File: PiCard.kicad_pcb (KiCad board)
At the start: 4 copper layers, 81 x 50 mm, 53 parts, among them J1 Usb Data Jumper, J2 USB_C_Receptacle_USB2.0_16P, J6 Micro_SD_Card_Det2, J7 nRPIBOOT Jumper, M2_3V3 TestPoint, U1 TPD4EUSB30, U3 TPD4EUSB30, U4 TPD4EUSB30, U5 MAX3232, U6 RT9742GGJ5, U7 TPS82130

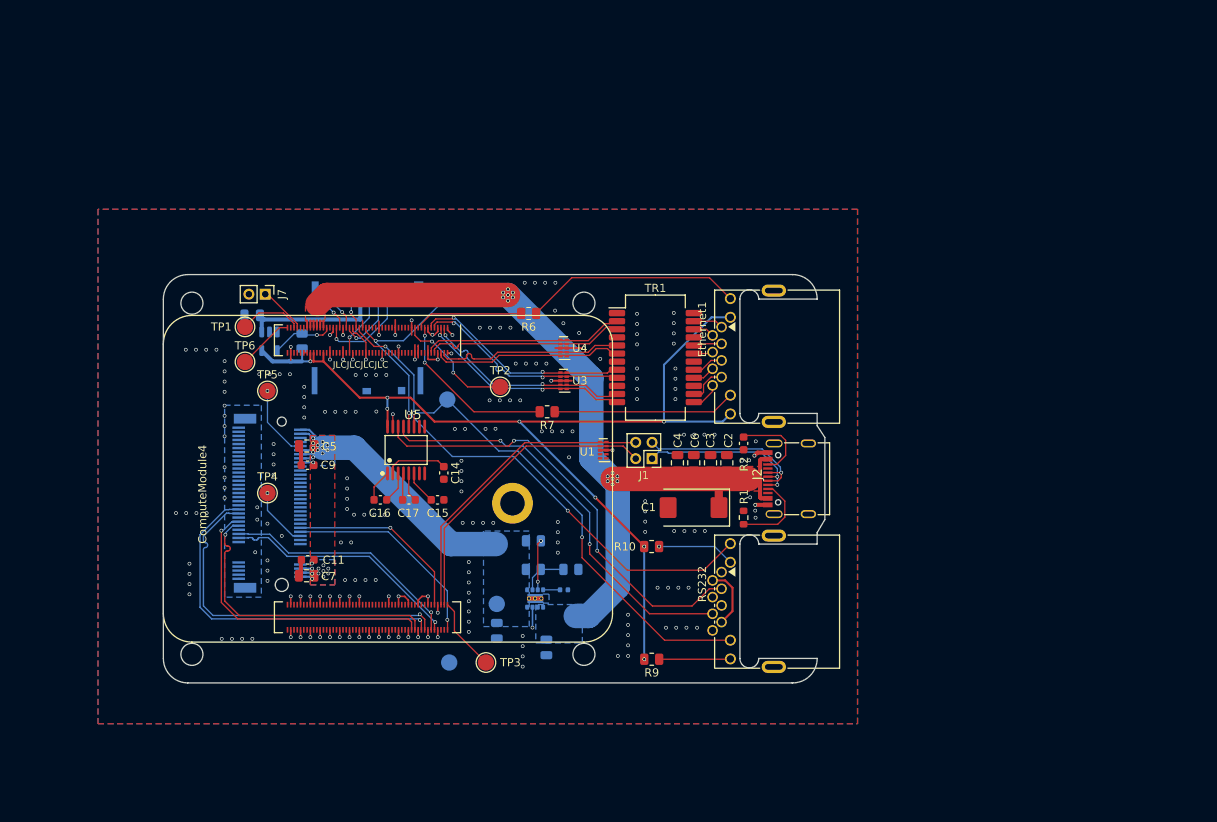
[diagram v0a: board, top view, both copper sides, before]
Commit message: Fix ethernet wiring order
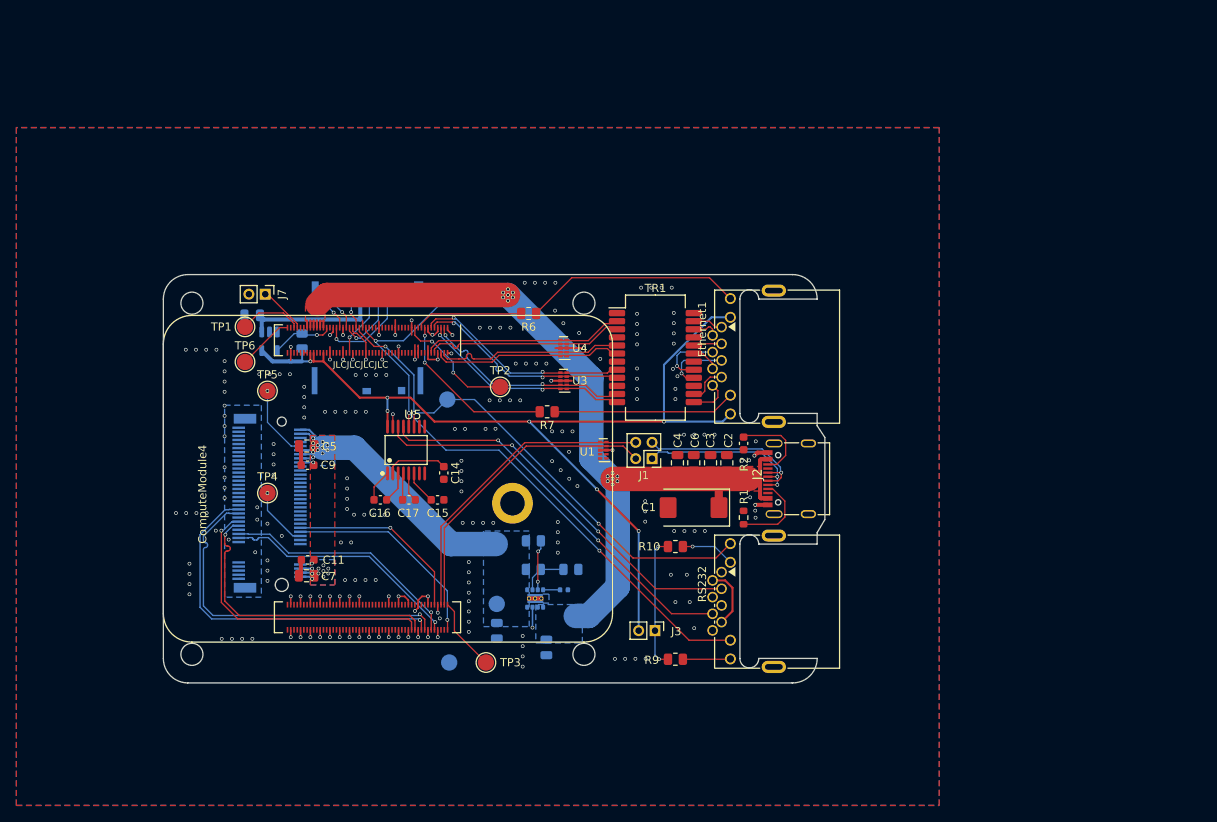
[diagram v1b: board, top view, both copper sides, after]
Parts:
- added J3: UART Activity Jumper, Connector_PinHeader_2.00mm:PinHeader_1x02_P2.00mm_Vertical, F.Cu at (120.2, 118.6)
- moved R10 2.91 mm to (122.7, 108.3), turned to 180 degrees
- moved R9 2.90 mm to (122.7, 122.1), turned to 0 degrees
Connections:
- net Net-(TR1-MX1+) renamed /Module A/DA_P
- net Net-(TR1-MX1-) renamed /Module A/DA_N
- net Net-(TR1-MX2+) renamed /Module A/DB_P
- net Net-(TR1-MX4+) renamed /Module A/DD_P
- net Net-(TR1-MX4-) renamed /Module A/DD_N
- Ethernet1 pad 4: Net-(TR1-MX2-) -> /Module A/DC_P
- Ethernet1 pad 5: Net-(TR1-MX3+) -> /Module A/DC_N
- Ethernet1 pad 6: Net-(TR1-MX3-) -> /Module A/DB_N
- R10 pad 1: +3.3V -> Net-(R10-Pad1)
- R10 pad 2: Net-(R10-Pad2) -> Net-(J3-Pin_1)
- R9 pad 1: Net-(R9-Pad1) -> Net-(J3-Pin_1)
- R9 pad 2: +3.3V -> Net-(R9-Pad2)
- RS232 pad 10: Net-(R9-Pad1) -> Net-(R9-Pad2)
- RS232 pad 11: /Module A/GPIO15_UART_RX -> /Module A/GPIO14_UART_TX
- RS232 pad 12: Net-(R10-Pad2) -> Net-(R10-Pad1)
- RS232 pad 9: /Module A/GPIO14_UART_TX -> /Module A/GPIO15_UART_RX
- TR1 pad 16: Net-(TR1-MX3-) -> /Module A/DC_N
- TR1 pad 17: Net-(TR1-MX3+) -> /Module A/DC_P
- TR1 pad 19: Net-(TR1-MX2-) -> /Module A/DB_N
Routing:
- net Net-(J3-Pin_1): track 0.00 -> 16.4 mm, vias 0 -> 2
- net Net-(R10-Pad2): track 9.53 -> 0.00 mm, vias 1 -> 0
- net Net-(R9-Pad1): track 8.78 -> 0.00 mm
- net /Module A/DC_P: track 0.00 -> 8.05 mm, vias 0 -> 1
- net /Module A/DC_N: track 0.00 -> 8.04 mm, vias 0 -> 1
- net Net-(R10-Pad1): track 0.00 -> 6.62 mm, vias 0 -> 1
- net /Module A/GPIO14_UART_TX: track 70.4 -> 63.9 mm
- net Net-(R9-Pad2): track 0.00 -> 5.88 mm
- net /Module A/RS232_TXD: track 53.9 -> 48.5 mm
- net +3.3V: track 122.7 -> 118.4 mm, vias 8 -> 7
- net Net-(TR1-MX3+): track 3.87 -> 0.00 mm
- net /Module A/DB_N: track 0.00 -> 3.45 mm
- net /Module A/RS232_RXD: track 50.9 -> 47.9 mm
- net Net-(TR1-MX3-): track 2.76 -> 0.00 mm
- net Net-(TR1-MX2-): track 2.37 -> 0.00 mm
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
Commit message: Clean up schematics
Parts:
- removed Ethernet1: Ethernet, PiCard:RJ45-TH_MJ88B-B011-RVL11-P
- removed PCIe1: Bus_M.2_Socket_M, PiCard:CONN-SMD_APCI0146-P001A
- removed RS232: RS232, PiCard:RJ45-TH_MJ88B-B011-RVL11-P
- added J4: Bus_M.2_Socket_M, PiCard:CONN-SMD_APCI0146-P001A, B.Cu at (73.0, 103.0)
- added J5: Ethernet, PiCard:RJ45-TH_MJ88B-B011-RVL11-P, F.Cu at (131.0, 85.0)
- added J8: RS232, PiCard:RJ45-TH_MJ88B-B011-RVL11-P, F.Cu at (131.0, 115.0)
- C11, C14, C15, C16, C17, C9: value 0.1uF -> 100nF
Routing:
- net Net-(RS232-Pad2): track 7.57 -> 0.00 mm
- net Net-(J8-Pad2): track 0.00 -> 7.57 mm

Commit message: PiCard v2
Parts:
- removed +5V1, GND1, GPIO14, GPIO15, M2_3V3, TP1, TP2, TP3, TP4, TP5, TP6: TestPoint, TestPoint:TestPoint_Pad_D2.0mm
- removed ComputeModule4: ComputeModule4-CM4, PiCard:Raspberry-Pi-4-Compute-Module
- removed J7: nRPIBOOT Jumper, Connector_PinHeader_2.00mm:PinHeader_1x02_P2.00mm_Vertical
- added BT1: RTC Battery, PiCard:BAT-SMD_MY-1220-03, F.Cu at (106.0, 90.0)
- added C13: 100n, Capacitor_SMD:C_0402_1005Metric, B.Cu at (163.2, 82.9)
- added C19: 22u, Capacitor_SMD:C_0805_2012Metric, B.Cu at (149.0, 71.5)
- added C20: 22u, Capacitor_SMD:C_0805_2012Metric, B.Cu at (151.7, 74.5)
- added C21: 430pF, Capacitor_SMD:C_0402_1005Metric, B.Cu at (146.5, 72.0)
- added C22: 100n, Capacitor_SMD:C_0402_1005Metric, B.Cu at (106.5, 92.5)
- added C23: 47u, Capacitor_SMD:C_0805_2012Metric, B.Cu at (113.0, 82.3)
- added C24: 47u, Capacitor_SMD:C_0805_2012Metric, B.Cu at (117.2, 72.9)
- added C25: 100n, Capacitor_SMD:C_0402_1005Metric, B.Cu at (119.4, 72.9)
- added C26: 100n, Capacitor_SMD:C_0402_1005Metric, B.Cu at (124.5, 72.9)
- added C27: 100n, Capacitor_SMD:C_0402_1005Metric, B.Cu at (113.5, 77.7)
- added C28: 100n, Capacitor_SMD:C_0402_1005Metric, B.Cu at (113.5, 76.7)
- added C29: 100n, Capacitor_SMD:C_0402_1005Metric, B.Cu at (133.0, 75.0)
- added C30: 100n, Capacitor_SMD:C_0402_1005Metric, B.Cu at (113.5, 72.6)
- added C31: 100n, Capacitor_SMD:C_0402_1005Metric, B.Cu at (113.5, 73.6)
- added C32: 2.2u, Capacitor_SMD:C_1206_3216Metric, F.Cu at (171.0, 70.5)
- added C33: 100n, Capacitor_SMD:C_0402_1005Metric, F.Cu at (111.6, 82.3)
- added C34: 100n, Capacitor_SMD:C_0402_1005Metric, B.Cu at (136.8, 56.8)
- added ComputeModule1: ComputeModule4-CM4, PiCard:Raspberry-Pi-4-Compute-Module, F.Cu at (116.8, 53.5)
- added D1: 1N5819WS, Diode_SMD:D_SOD-323, B.Cu at (140.0, 68.8)
- added D3: 1N5819WS, Diode_SMD:D_SOD-323, B.Cu at (142.8, 60.0)
- added D4: LED_Dual_AAKK, PiCard:LED-ARRAY-SMD_4P-L3.0-W1.5-L-FD, B.Cu at (137.3, 51.5)
- added H1: MountingHole, PiCard:MOUNTING-HOLE, F.Cu at (116.8, 96.5)
- added H2: MountingHole, PiCard:MOUNTING-HOLE, F.Cu at (164.8, 96.5)
- added JP1: SolderJumper_2_Open, Jumper:SolderJumper-2_P1.3mm_Open_TrianglePad1.0x1.5mm, F.Cu at (170.5, 77.2)
- added L1: 1u, Inductor_SMD:L_1008_2520Metric, B.Cu at (164.9, 73.3)
- added L2: 1u, Inductor_SMD:L_1008_2520Metric, B.Cu at (154.8, 73.3)
- added Q2: DMP3013SFV, Package_SON:Diodes_PowerDI3333-8, F.Cu at (170.9, 74.0)
- added R13: 5.1k, Resistor_SMD:R_0402_1005Metric, B.Cu at (157.5, 80.0)
- added R14: 1k, Resistor_SMD:R_0402_1005Metric, B.Cu at (157.5, 81.0)
- added R15: 150k 1%, Resistor_SMD:R_0402_1005Metric, B.Cu at (162.0, 70.6)
- added R16: 15.8k, Resistor_SMD:R_0402_1005Metric, B.Cu at (108.4, 85.7)
- added R21: 15.8k, Resistor_SMD:R_0402_1005Metric, B.Cu at (142.5, 58.1)
- added R22: 309k, Resistor_SMD:R_0402_1005Metric, B.Cu at (146.5, 75.3)
- added R23: 49.9k, Resistor_SMD:R_0402_1005Metric, B.Cu at (157.0, 76.5)
- added R24: 100k 1%, Resistor_SMD:R_0402_1005Metric, B.Cu at (145.5, 75.3)
- added R25: 1k, Resistor_SMD:R_0402_1005Metric, B.Cu at (157.0, 78.5)
- added R26: 5.1k, Resistor_SMD:R_0402_1005Metric, B.Cu at (135.0, 66.0)
- added R27: 5.1k, Resistor_SMD:R_0402_1005Metric, B.Cu at (134.0, 66.0)
- added R28: 12k, Resistor_SMD:R_0402_1005Metric, B.Cu at (113.6, 84.3)
- added R29: 909k, Resistor_SMD:R_0402_1005Metric, B.Cu at (122.0, 76.0)
- added R30: 12k, Resistor_SMD:R_0402_1005Metric, B.Cu at (127.5, 73.0)
- added R31: 200k, Resistor_SMD:R_0402_1005Metric, B.Cu at (119.0, 80.5)
- added R32: 200k, Resistor_SMD:R_0402_1005Metric, B.Cu at (121.8, 72.9)
- added R33: 499k, Resistor_SMD:R_0402_1005Metric, B.Cu at (120.8, 72.9)
- added R34: 12k, Resistor_SMD:R_0402_1005Metric, B.Cu at (118.0, 80.5)
- added R35: 12k, Resistor_SMD:R_0402_1005Metric, B.Cu at (130.0, 72.0)
- added R36: 1k, Resistor_SMD:R_0402_1005Metric, B.Cu at (142.3, 51.5)
- added SW1: SW_DIP_x04, PiCard:SW-SMD_8P-P1.27_EU-04KS, B.Cu at (126.5, 68.5)
- added SYM1: PiCard v2.1, PiCard:PICARD_NAMEPLATE, F.Cu at (144.0, 95.0)
- added U10: ~, Package_TO_SOT_SMD:SOT-23-6, B.Cu at (111.0, 85.0)
- added U11: TPD4EUSB30, Package_SON:USON-10_2.5x1.0mm_P0.5mm, B.Cu at (170.0, 78.5)
- added U12: TPD4EUSB30, Package_SON:USON-10_2.5x1.0mm_P0.5mm, F.Cu at (111.0, 75.5)
- added U13: TPD4EUSB30, Package_SON:USON-10_2.5x1.0mm_P0.5mm, B.Cu at (111.0, 77.9)
- added U14: TPD4EUSB30, Package_SON:USON-10_2.5x1.0mm_P0.5mm, B.Cu at (111.0, 73.9)
- added U15: TS3USB221, Package_DFN_QFN:Texas_UQFN-10_1.5x2mm_P0.5mm, B.Cu at (130.5, 75.0)
- added U16: HD3SS3220, PiCard:RNH0030A, B.Cu at (118.0, 76.5)
- added U17: TS3USB221, Package_DFN_QFN:Texas_UQFN-10_1.5x2mm_P0.5mm, B.Cu at (125.0, 75.0)
- added U18: 74LVC1G07, Package_TO_SOT_SMD:SOT-353_SC-70-5, B.Cu at (143.0, 56.0)
- added U2: SN74AHC123A, Package_SO:TSSOP-16_4.4x5mm_P0.65mm, B.Cu at (139.5, 64.0)
- added U8: TPS82130, PiCard:Texas_SIL0008D_MicroSiP-8-1EP_2.8x3mm_P0.65mm_EP1.1x1.9mm_ThermalVias, B.Cu at (149.0, 74.5)
- added U9: DS1307Z+, Package_SO:SOIC-8_3.9x4.9mm_P1.27mm, B.Cu at (104.0, 89.0)
- added Y1: 32.768kHz, Crystal:Crystal_SMD_3215-2Pin_3.2x1.5mm, B.Cu at (102.5, 93.0)
- C1: value 100uF -> 100n; footprint Capacitor_Tantalum_SMD:CP_EIA-7343-31_Kemet-D -> Capacitor_SMD:C_0402_1005Metric; moved to B.Cu
- C10: value 430pF -> 1u; footprint Capacitor_SMD:C_0402_1005Metric -> Capacitor_SMD:C_0603_1608Metric
- C11: value 100nF -> 1u; moved to B.Cu
- C12: value 22uF -> 100n; footprint Capacitor_SMD:C_0805_2012Metric -> Capacitor_SMD:C_0402_1005Metric
- C14, C15: value 100nF -> 22u; footprint Capacitor_SMD:C_0603_1608Metric -> Capacitor_SMD:C_0805_2012Metric; moved to B.Cu
- C16, C17: value 100nF -> 47u; footprint Capacitor_SMD:C_0603_1608Metric -> Capacitor_SMD:C_0805_2012Metric; moved to B.Cu
- C18: value 10uF -> 22n; footprint Capacitor_SMD:C_0805_2012Metric -> Capacitor_SMD:C_0603_1608Metric
- C2, C3, C4, C5, C7: value 10u -> 100n; footprint Capacitor_SMD:C_0805_2012Metric -> Capacitor_SMD:C_0402_1005Metric; moved to B.Cu
- C6: value 10u -> 1u; footprint Capacitor_SMD:C_0805_2012Metric -> Capacitor_SMD:C_0603_1608Metric; moved to B.Cu
- C8: value 22uF -> 1u; footprint Capacitor_SMD:C_0805_2012Metric -> Capacitor_SMD:C_0603_1608Metric
- C9: value 100nF -> 10u; footprint Capacitor_SMD:C_0603_1608Metric -> Capacitor_SMD:C_0805_2012Metric; moved to B.Cu
- J1: value Usb Data Jumper -> RS232; footprint Connector_PinHeader_2.00mm:PinHeader_2x02_P2.00mm_Vertical -> PiCard:RJ45-TH_RJ45-005-202-11
- J2: value USB_C_Receptacle_USB2.0_16P -> Ethernet; footprint PiCard:USB-C-SMD_TYPEC-304J-BCP16 -> PiCard:RJ45-TH_RJ45-005-202-11
- J3: value UART Activity Jumper -> Micro_SD_Card_Det2; footprint Connector_PinHeader_2.00mm:PinHeader_1x02_P2.00mm_Vertical -> PiCard:TF-SMD_503398-1892; moved to B.Cu
- J5: value Ethernet -> USB_C_Receptacle; footprint PiCard:RJ45-TH_MJ88B-B011-RVL11-P -> PiCard:USB-C-SMD_TYPE-C-31-M-27
- J6: value Micro_SD_Card_Det2 -> USB_C_Receptacle; footprint PiCard:TF-SMD_503398-1892 -> PiCard:USB-C-SMD_TYPE-C-31-M-27; moved to F.Cu
- J8: value RS232 -> HDMI_C_1.4; footprint PiCard:RJ45-TH_MJ88B-B011-RVL11-P -> PiCard:HDMI-SMD_19P-P0.40-H-F_HDMI-519S
- R1: value 5.1K -> 470; footprint Resistor_SMD:R_0603_1608Metric -> Resistor_SMD:R_0402_1005Metric; moved to B.Cu
- R10: value 470R -> 787k; footprint Resistor_SMD:R_0805_2012Metric -> Resistor_SMD:R_0402_1005Metric; moved to B.Cu
- R2: value 5.1K -> 470; footprint Capacitor_SMD:C_0603_1608Metric -> Resistor_SMD:R_0402_1005Metric; moved to B.Cu
- R3: value 100k -> 1k; footprint Resistor_SMD:R_0805_2012Metric -> Resistor_SMD:R_0402_1005Metric
- R4: value 309k -> 100k 1%; footprint Resistor_SMD:R_0805_2012Metric -> Resistor_SMD:R_0402_1005Metric
- R5: value 100k -> 100k 1%; footprint Resistor_SMD:R_0805_2012Metric -> Resistor_SMD:R_0402_1005Metric
- R6, R7: value 470R -> 470; footprint Resistor_SMD:R_0805_2012Metric -> Resistor_SMD:R_0402_1005Metric; moved to B.Cu
- R8: value 12K 1% -> 12k; footprint Resistor_SMD:R_0805_2012Metric -> Resistor_SMD:R_0402_1005Metric
- R9: value 470R -> 12k; footprint Resistor_SMD:R_0805_2012Metric -> Resistor_SMD:R_0402_1005Metric
- TR1: value 30F-51NL -> H2456G; footprint Transformer_SMD:Transformer_Ethernet_YDS_30F-51NL_SO-24_7.1x15.1mm -> PiCard:XFMR-SMD-24_L16.6-W9.0-LS9.6-BL; moved to B.Cu
- U1: value TPD4EUSB30 -> MAX3232; footprint Package_SON:USON-10_2.5x1.0mm_P0.5mm -> Package_SO:TSSOP-16_4.4x5mm_P0.65mm; moved to B.Cu
- U3, U4: moved to B.Cu
- U5: value MAX3232 -> ~; footprint PiCard:TSSOP-16_L5.0-W4.4-P0.65-LS6.4-BL -> Package_TO_SOT_SMD:SOT-23-6; moved to B.Cu
- U6: value RT9742GGJ5 -> TPS62180; footprint Package_TO_SOT_SMD:TSOT-23-5 -> PiCard:YZF0024AMAM
- U7: value TPS82130 -> CYPD3177-24LQ; footprint PiCard:Texas_SIL0008D_MicroSiP-8-1EP_2.8x3mm_P0.65mm_EP1.1x1.9mm_ThermalVias -> Package_DFN_QFN:QFN-24-1EP_4x4mm_P0.5mm_EP2.75x2.75mm
- moved J6 92.1 mm to (176.8, 75.0), turned to 90 degrees
- moved C18 89.4 mm to (159.7, 70.0), turned to 90 degrees
- moved U6 87.5 mm to (159.9, 73.3), turned to 90 degrees
- moved C11 87.4 mm to (161.0, 83.5), turned to 90 degrees
- moved C16 85.1 mm to (165.3, 70.3)
- moved C7 82.2 mm to (144.0, 63.5), turned to 90 degrees
- moved C14 72.9 mm to (162.5, 73.5), turned to 90 degrees
- moved C17 72.0 mm to (154.4, 70.3), turned to 180 degrees
- moved C12 71.0 mm to (162.2, 82.9), turned to 90 degrees
- moved C9 70.5 mm to (136.5, 59.5), turned to -90 degrees
- moved C15 69.9 mm to (157.2, 73.5), turned to 90 degrees
- moved C8 68.7 mm to (138.3, 59.5), turned to 90 degrees
- moved U7 66.4 mm to (161.5, 79.0), turned to 0 degrees
- moved R3 66.4 mm to (142.3, 52.5), turned to 180 degrees
- moved R8 64.4 mm to (135.8, 56.8), turned to -90 degrees
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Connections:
- C1 pad 1: +5V -> GND
- C1 pad 2: GND -> +3.3V
- C10 pad 2: Net-(U7-SS/TR) -> Net-(U7-VCCD)
- C11 pad 1: /Module B/M2_3V3 -> GND
- C11 pad 2: GND -> /Power/CYPD3177_3V3
- C12 pad 1: /Module B/M2_3V3 -> GND
- C12 pad 2: GND -> /Power/CYPD3177_3V3
- C14 pad 1: Net-(U5-VS+) -> VBUS
- C15 pad 1: Net-(U5-VS-) -> VBUS
- C16 pad 1: Net-(U5-C1+) -> +5V
- C16 pad 2: Net-(U5-C1-) -> GND
- C17 pad 1: Net-(U5-C2+) -> +5V
- C17 pad 2: Net-(U5-C2-) -> GND
- C18 pad 1: /Module A/SD_PWR -> Net-(U6-SS)
- C2 pad 1: +5V -> Net-(U1-C1+)
- C2 pad 2: GND -> Net-(U1-C1-)
- C3 pad 1: +5V -> Net-(U1-C2+)
- C3 pad 2: GND -> Net-(U1-C2-)
- C4 pad 1: +5V -> Net-(U1-VS+)
- C5 pad 1: GND -> Net-(U1-VS-)
- C5 pad 2: /Module B/M2_3V3 -> GND
- C6 pad 1: +5V -> Net-(D1-A)
- C7 pad 2: /Module B/M2_3V3 -> +3.3V
- C8 pad 1: +5V -> Net-(D3-A)
- C9 pad 1: /Module B/M2_3V3 -> /Module A/SD_PWR
- J1 pad 2: /Module B/USB2_N -> Net-(J1-Pad2)
- J1 pad 3: /Module B/TYPEC_D_P -> /Module A/RS232_TXD
- J1 pad 4: /Module B/USB2_P -> GND
- J3 pad 1: Net-(J3-Pin_1) -> /Module A/SD_DAT2
- J3 pad 2: +3.3V -> /Module A/SD_DAT3
- J4 pad 10: /Module B/M2_LED -> unconnected-(J4-DAS/~{DSS}/~{LED1}-Pad10)
- J4 pad 12: /Module B/M2_3V3 -> M2_3.3V
- J4 pad 14: /Module B/M2_3V3 -> M2_3.3V
- J4 pad 16: /Module B/M2_3V3 -> M2_3.3V
- J4 pad 18: /Module B/M2_3V3 -> M2_3.3V
- J4 pad 2: /Module B/M2_3V3 -> M2_3.3V
- J4 pad 4: /Module B/M2_3V3 -> M2_3.3V
- J4 pad 54: /Module B/PEWAKE -> Net-(J4-~{PEWAKE})
- J4 pad 70: /Module B/M2_3V3 -> M2_3.3V
- J4 pad 72: /Module B/M2_3V3 -> M2_3.3V
- J4 pad 74: /Module B/M2_3V3 -> M2_3.3V
- J8 pad 1: unconnected-(J8-Pad1) -> GND
- J8 pad 10: Net-(J8-Pad10) -> GND
- J8 pad 11: /Module A/GPIO14_UART_TX -> /Module B/HDMI0_CLK_P
- J8 pad 12: Net-(J8-Pad12) -> /Module B/HDMI0_CLK_N
- J8 pad 2: Net-(J8-Pad2) -> /Module B/HDMI0_TX2_P
- J8 pad 3: /Module A/RS232_TXD -> /Module B/HDMI0_TX2_N
- J8 pad 5: GND -> /Module B/HDMI0_TX1_P
- J8 pad 6: /Module A/RS232_RXD -> /Module B/HDMI0_TX1_N
- J8 pad 7: Net-(J8-Pad2) -> GND
- J8 pad 8: unconnected-(J8-Pad8) -> /Module B/HDMI0_TX0_P
- J8 pad 9: /Module A/GPIO15_UART_RX -> /Module B/HDMI0_TX0_N
- R1 pad 1: Net-(J2-CC1) -> Net-(J1-Pad12)
- R1 pad 2: GND -> /Module A/UART_TX_ACT
- R10 pad 1: Net-(J8-Pad12) -> +5V
- R10 pad 2: Net-(J3-Pin_1) -> Net-(U6-FB)
- R2 pad 1: GND -> /Module A/UART_RX_ACT
- R2 pad 2: Net-(J2-CC2) -> Net-(J1-Pad10)
- R3 pad 1: /Module B/M2_3V3 -> /Module A/GREEN_LED_K
- R3 pad 2: Net-(U7-PG) -> Net-(D4-K2)
- R4 pad 1: /Module B/M2_3V3 -> +3.3V
- R4 pad 2: Net-(U7-FB) -> Net-(D1-A)
- R5 pad 1: GND -> +3.3V
- R5 pad 2: Net-(U7-FB) -> Net-(D3-A)
- R6 pad 1: Net-(J5-Pad11) -> Net-(J2-Pad11)
- R7 pad 1: Net-(J5-Pad9) -> Net-(J2-Pad9)
- R8 pad 1: +3.3V -> /Module A/SD_PWR_ON
- R8 pad 2: /Module A/SD_PWR_ON -> +3.3V
- R9 pad 1: Net-(J3-Pin_1) -> Net-(J4-~{PEWAKE})
- R9 pad 2: Net-(J8-Pad10) -> M2_3.3V
- TR1 pad 11: /Module A/TRD3_P -> /Module A/DD_N
- TR1 pad 12: /Module A/TRD3_N -> /Module A/DD_P
- TR1 pad 13: /Module A/DD_N -> /Module A/TRD3_P
- TR1 pad 14: /Module A/DD_P -> /Module A/TRD3_N
- TR1 pad 16: /Module A/DC_N -> /Module A/TRD2_P
- TR1 pad 17: /Module A/DC_P -> /Module A/TRD2_N
- TR1 pad 19: /Module A/DB_N -> /Module A/TRD1_P
- TR1 pad 2: /Module A/TRD0_P -> /Module A/DA_N
- TR1 pad 20: /Module A/DB_P -> /Module A/TRD1_N
- TR1 pad 22: /Module A/DA_N -> /Module A/TRD0_P
- TR1 pad 23: /Module A/DA_P -> /Module A/TRD0_N
- TR1 pad 3: /Module A/TRD0_N -> /Module A/DA_P
- TR1 pad 5: /Module A/TRD1_P -> /Module A/DB_N
- TR1 pad 6: /Module A/TRD1_N -> /Module A/DB_P
- TR1 pad 8: /Module A/TRD2_P -> /Module A/DC_N
- TR1 pad 9: /Module A/TRD2_N -> /Module A/DC_P
- U1 pad 1: unconnected-(U1-D1+-Pad1) -> Net-(U1-C1+)
- U1 pad 2: unconnected-(U1-D1--Pad2) -> Net-(U1-VS+)
- U1 pad 3: GND -> Net-(U1-C1-)
- U1 pad 4: /Module B/USB2_N -> Net-(U1-C2+)
- U1 pad 5: /Module B/USB2_P -> Net-(U1-C2-)
- U1 pad 6: /Module B/USB2_P -> Net-(U1-VS-)
- U1 pad 7: /Module B/USB2_N -> unconnected-(U1-T2OUT-Pad7)
- U1 pad 8: GND -> unconnected-(U1-R2IN-Pad8)
- U3 pad 1: /Module A/TRD3_N -> /Module A/TRD3_P
- U3 pad 10: /Module A/TRD3_N -> /Module A/TRD3_P
- U3 pad 2: /Module A/TRD3_P -> /Module A/TRD3_N
- U3 pad 4: /Module A/TRD2_N -> /Module A/TRD2_P
- U3 pad 5: /Module A/TRD2_P -> /Module A/TRD2_N
- U3 pad 6: /Module A/TRD2_P -> /Module A/TRD2_N
- U3 pad 7: /Module A/TRD2_N -> /Module A/TRD2_P
- U3 pad 9: /Module A/TRD3_P -> /Module A/TRD3_N
- U4 pad 1: /Module A/TRD1_N -> /Module A/TRD0_N
- U4 pad 10: /Module A/TRD1_N -> /Module A/TRD0_N
- U4 pad 2: /Module A/TRD1_P -> /Module A/TRD0_P
- U4 pad 4: /Module A/TRD0_N -> /Module A/TRD1_N
- U4 pad 5: /Module A/TRD0_P -> /Module A/TRD1_P
- U4 pad 6: /Module A/TRD0_P -> /Module A/TRD1_P
- U4 pad 7: /Module A/TRD0_N -> /Module A/TRD1_N
- U4 pad 9: /Module A/TRD1_P -> /Module A/TRD0_P
- U5 pad 1: Net-(U5-C1+) -> +3.3V
- U5 pad 2: Net-(U5-VS+) -> GND
- U5 pad 3: Net-(U5-C1-) -> /Module A/SD_PWR_ON
- U5 pad 4: Net-(U5-C2+) -> unconnected-(U5-~{FAULT}-Pad4)
- U5 pad 5: Net-(U5-C2-) -> Net-(U5-ILM)
- U5 pad 6: Net-(U5-VS-) -> /Module A/SD_PWR
- U7 pad 1: +5V -> GND
- U7 pad 2: +5V -> Net-(U7-VBUS_MAX)
- U7 pad 3: GND -> /Power/VBUS_FET_EN
- U7 pad 4: /Module B/M2_3V3 -> unconnected-(U7-SAFE_PWR_EN-Pad4)
- U7 pad 5: /Module B/M2_3V3 -> GND
- U7 pad 6: Net-(U7-FB) -> /Power/CYPD3177_3V3
- U7 pad 7: Net-(U7-PG) -> unconnected-(U7-~{HPI_INT}-Pad7)
- U7 pad 8: Net-(U7-SS/TR) -> unconnected-(U7-GPIO_1-Pad8)
- U7 pad 9: GND -> unconnected-(U7-FAULT-Pad9)
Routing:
- net GND: track 83.2 -> 248.8 mm, vias 229 -> 172
- net RTC_SCL: track 0.00 -> 63.2 mm, vias 0 -> 5
- net RTC_SDA: track 0.00 -> 62.3 mm, vias 0 -> 5
- net M2_3.3V: track 0.00 -> 61.3 mm, vias 0 -> 2
- net /Module A/UART_RX_ACT: track 0.00 -> 54.1 mm, vias 0 -> 2
- net /USB/RIGHT_USB2_P: track 0.00 -> 51.2 mm, vias 0 -> 3
- net /USB/RIGHT_USB2_N: track 0.00 -> 51.0 mm, vias 0 -> 4
- net +5V: track 104.0 -> 152.5 mm, vias 14 -> 22
- net /Module A/GPIO15_UART_RX: track 76.6 -> 30.7 mm, vias 3 -> 6
- net +3.3V: track 118.4 -> 163.0 mm, vias 7 -> 13
- net /Module B/M2_3V3: track 42.2 -> 0.00 mm, vias 24 -> 0
- net /Module A/UART_TX_ACT: track 0.00 -> 41.0 mm, vias 0 -> 2
- net Net-(ComputeModule1A-nPI_LED_PWR): track 0.00 -> 37.9 mm, vias 0 -> 3
- net /Module B/USB2_P: track 37.7 -> 0.00 mm
- net /Module B/USB2_N: track 37.6 -> 0.00 mm
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- added copper zone on B.Cu, net /USB/USB3_VBUS
- added copper zone on In1.Cu, net /USB/USB3_VBUS
- added copper zone on In2.Cu, net /USB/USB3_VBUS
- added copper zone on B.Cu, net M2_3.3V
- added copper zone on F.Cu, net PD_VBUS
- added copper zone on B.Cu, net VBUS
- added copper zone on F.Cu, net VBUS
- removed copper zone on B.Cu, net +5V
- removed copper zone on B.Cu, net /Module B/M2_3V3
- removed copper zone on F.Cu, net /Module B/M2_3V3
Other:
- board size 81 x 50 mm -> 81.5 x 50 mm
- board text added: "Ethernet"
- board text added: "OFF OFF OFF OFF"
- board text added: "ON ON ON ON"
- board text added: "RS232"
- board text added: "USB3 USB2 RPIBOOT RS232 LED"
- board text added: "V-CUT"

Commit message: PiCard v2.2
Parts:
- removed R28: 12k, Resistor_SMD:R_0402_1005Metric
- added R11: 200k, Resistor_SMD:R_0402_1005Metric, B.Cu at (113.6, 84.3)
- SYM1: value PiCard v2.1 -> PiCard v2.2
- U10: value ~ -> TPS2552
- U5: value ~ -> TPS2553
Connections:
- U10 pad 3: Net-(U10-EN) -> /USB/ID
- U16 pad 27: unconnected-(U16-ID-Pad27) -> /USB/ID
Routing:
- net /USB/ID: track 0.00 -> 29.3 mm
- net +5V: track 152.5 -> 148.6 mm
- net Net-(U10-EN): track 2.34 -> 0.00 mm
- net GND: track 248.8 -> 251.0 mm, vias 172 -> 174

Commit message: PiCard v3.0
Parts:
- removed the C10 at (159.5, 83.5)
- removed the C11 at (161.0, 83.5)
- removed the C12 at (162.2, 82.9)
- removed the C13 at (163.2, 82.9)
- removed the C5 at (135.0, 71.0)
- removed J8: HDMI_C_1.4, PiCard:HDMI-SMD_19P-P0.40-H-F_HDMI-519S
- removed JP1: SolderJumper_2_Open, Jumper:SolderJumper-2_P1.3mm_Open_TrianglePad1.0x1.5mm
- removed the R11 at (113.6, 84.3)
- removed the R13 at (157.5, 80.0)
- removed the R3 at (142.3, 52.5)
- removed the R8 at (135.8, 56.8)
- removed the U7 at (161.5, 79.0)
- added C17: 100n, Capacitor_SMD:C_0402_1005Metric, B.Cu at (159.0, 87.5)
- added C18: 10u, Capacitor_SMD:C_0805_2012Metric, B.Cu at (158.5, 84.5)
- added C19: 2.2n, Capacitor_SMD:C_0402_1005Metric, B.Cu at (127.5, 75.5)
- added C20: 2.2n, Capacitor_SMD:C_0402_1005Metric, B.Cu at (157.0, 76.0)
- added C21: 100n, Capacitor_SMD:C_0402_1005Metric, B.Cu at (115.5, 91.0)
- added C35: 100n, Capacitor_SMD:C_0402_1005Metric, B.Cu at (114.0, 75.7)
- added C36: 100n, Capacitor_SMD:C_0402_1005Metric, B.Cu at (167.5, 74.0)
- added C37: 100n, Capacitor_SMD:C_0402_1005Metric, B.Cu at (114.0, 76.7)
- added C38: 100n, Capacitor_SMD:C_0402_1005Metric, B.Cu at (167.5, 75.0)
- added C39: 100n, Capacitor_SMD:C_0402_1005Metric, B.Cu at (117.6, 80.5)
- added C40: 100n, Capacitor_SMD:C_0402_1005Metric, B.Cu at (157.5, 78.0)
- added C41: 100n, Capacitor_SMD:C_0402_1005Metric, B.Cu at (163.0, 83.0)
- added C42: 4.7u, Capacitor_SMD:C_0603_1608Metric, B.Cu at (142.7, 57.3)
- added C43: 100n, Capacitor_SMD:C_0402_1005Metric, B.Cu at (142.9, 59.3)
- added C44: 1u, Capacitor_SMD:C_0603_1608Metric, B.Cu at (141.2, 58.3)
- added C45: 18pf, Capacitor_SMD:C_0402_1005Metric, B.Cu at (137.0, 56.8)
- added C46: 100n, Capacitor_SMD:C_0402_1005Metric, B.Cu at (129.3, 67.6)
- added C47: 1u, Capacitor_SMD:C_0603_1608Metric, B.Cu at (134.0, 66.5)
- added C48: 18pf, Capacitor_SMD:C_0402_1005Metric, B.Cu at (139.0, 56.8)
- added C49: 4.7u 50V, Capacitor_SMD:C_0805_2012Metric, F.Cu at (109.5, 79.5)
- added C50: 4.7u 50V, Capacitor_SMD:C_0805_2012Metric, F.Cu at (172.0, 78.5)
- added C51: 100n, Capacitor_SMD:C_0402_1005Metric, F.Cu at (165.2, 91.2)
- added D10: WS2812B, PiCard:LED-SMD_4P-L4.0-W1.7-R, B.Cu at (143.0, 52.0)
- added D11: WS2812B, PiCard:LED-SMD_4P-L4.0-W1.7-R, B.Cu at (148.0, 52.0)
- added D12: WS2812B, PiCard:LED-SMD_4P-L4.0-W1.7-R, B.Cu at (153.0, 52.0)
- added D13: D, Diode_SMD:D_SOD-323, B.Cu at (142.8, 70.8)
- added D3: 1N5819WS, Diode_SMD:D_SOD-323, B.Cu at (138.0, 74.5)
- added D5: D, Diode_SMD:D_SOD-323, B.Cu at (159.0, 69.5)
- added D6: D, Diode_SMD:D_SOD-323, B.Cu at (123.2, 66.3)
- added D7: Zener 20V, Diode_SMD:D_SOD-323, B.Cu at (126.7, 66.3)
- added D8: 1N5819WS, Diode_SMD:D_SOD-323, B.Cu at (162.5, 69.5)
- added D9: 1N5819WS, Diode_SMD:D_SOD-323, B.Cu at (120.0, 74.0)
- added J7: Conn_02x05_Odd_Even, PiCard:HARWIN_M20-7810545R, F.Cu at (153.4, 95.0)
- added Q1: DMN32D2LFB4, Package_DFN_QFN:Diodes_DFN1006-3, B.Cu at (109.0, 85.0)
- added Q3: DMN32D2LFB4, Package_DFN_QFN:Diodes_DFN1006-3, B.Cu at (111.5, 96.0)
- added Q4: DMN32D2LFB4, Package_DFN_QFN:Diodes_DFN1006-3, B.Cu at (119.6, 84.6)
- added Q5: DMN32D2LFB4, Package_DFN_QFN:Diodes_DFN1006-3, B.Cu at (162.3, 78.0)
- added R15: 220k 1%, Resistor_SMD:R_0402_1005Metric, B.Cu at (122.0, 70.5)
- added R17: 59k, Resistor_SMD:R_0402_1005Metric, B.Cu at (122.0, 73.0)
- added R18: 59k, Resistor_SMD:R_0402_1005Metric, B.Cu at (161.0, 71.5)
- added R19: 28.7k, Resistor_SMD:R_0402_1005Metric, B.Cu at (123.0, 75.5)
- added R20: 28.7k, Resistor_SMD:R_0402_1005Metric, B.Cu at (161.0, 73.5)
- added R22: 953, Resistor_SMD:R_0402_1005Metric, B.Cu at (155.0, 76.0)
- added R24: 953, Resistor_SMD:R_0402_1005Metric, B.Cu at (157.0, 68.5)
- added R28: 120k, Resistor_SMD:R_0402_1005Metric, B.Cu at (165.5, 67.0)
- added R37: 3.3k, Resistor_SMD:R_0402_1005Metric, B.Cu at (146.5, 64.5)
- added R38: 3.3k, Resistor_SMD:R_0402_1005Metric, B.Cu at (146.5, 66.5)
- added R39: 12k, Resistor_SMD:R_0402_1005Metric, B.Cu at (117.3, 78.1)
- added R40: 12k, Resistor_SMD:R_0402_1005Metric, B.Cu at (160.5, 78.0)
- added R41: 12k, Resistor_SMD:R_0402_1005Metric, F.Cu at (143.5, 92.5)
- added R7: 12k, Resistor_SMD:R_0402_1005Metric, B.Cu at (139.4, 55.6)
- added R9: 3.3k, Resistor_SMD:R_0402_1005Metric, F.Cu at (128.0, 95.0)
- added SW2: SW_DIP_x04, PiCard:SW-SMD_8P-L11.1-W6.2-P2.54-LS7.8, F.Cu at (135.0, 95.0)
- added TP1: TestPoint, TestPoint:TestPoint_Pad_D1.5mm, B.Cu at (148.6, 54.5)
- added TP2: TestPoint, TestPoint:TestPoint_Pad_D1.5mm, B.Cu at (147.1, 68.8)
- added TP3: TestPoint, TestPoint:TestPoint_Pad_D1.5mm, B.Cu at (138.4, 70.6)
- added TP4: TestPoint, TestPoint:TestPoint_Pad_D1.5mm, B.Cu at (135.0, 69.2)
- added TP5: TestPoint, TestPoint:TestPoint_Pad_D1.5mm, B.Cu at (145.7, 54.7)
- added TP6: TestPoint, TestPoint:TestPoint_Pad_D1.5mm, B.Cu at (140.0, 80.5)
- added TP7: TestPoint, TestPoint:TestPoint_Pad_D1.5mm, B.Cu at (136.5, 80.5)
- added TP8: TestPoint, TestPoint:TestPoint_Pad_D1.5mm, B.Cu at (144.0, 79.0)
- added U14: AP21510, Package_DFN_QFN:DFN-6-1EP_2x1.8mm_P0.5mm_EP1.2x1.6mm, B.Cu at (119.2, 90.5)
- added U20: TPD4EUSB30, Package_SON:USON-10_2.5x1.0mm_P0.5mm, B.Cu at (112.1, 77.0)
- added U21: TPD4EUSB30, Package_SON:USON-10_2.5x1.0mm_P0.5mm, B.Cu at (169.5, 73.5)
- added U22: TPD6S300A, Package_DFN_QFN:WQFN-20-1EP_3x3mm_P0.4mm_EP1.7x1.7mm_ThermalVias, B.Cu at (165.8, 81.1)
- added U23: TPD6S300A, Package_DFN_QFN:WQFN-20-1EP_3x3mm_P0.4mm_EP1.7x1.7mm_ThermalVias, B.Cu at (113.0, 81.5)
- added U24: FUSB340TMX, PiCard:QFN-18-1EP_2x2.8mm_P0.4mm_EP1.05x1.85mm, B.Cu at (116.5, 75.8)
- added U25: FUSB340TMX, PiCard:QFN-18-1EP_2x2.8mm_P0.4mm_EP1.05x1.85mm, B.Cu at (164.6, 74.8)
- added U26: TS3USB221, PiCard:RSE10, B.Cu at (117.0, 82.5)
- added U27: TS3USB221, PiCard:RSE10, B.Cu at (158.0, 81.0)
- added U28: TS3USB221, PiCard:RSE10, B.Cu at (161.8, 80.8)
- added U29: TLV70433, Package_TO_SOT_SMD:SOT-23-5, B.Cu at (131.5, 67.1)
- added U30: STM32G071CBUx, Package_DFN_QFN:QFN-48-1EP_7x7mm_P0.5mm_EP5.6x5.6mm, B.Cu at (141.5, 64.0)
- added U8: AP21510, Package_DFN_QFN:DFN-6-1EP_2x1.8mm_P0.5mm_EP1.2x1.6mm, B.Cu at (161.0, 84.3)
- BT1: value RTC Battery -> CR1220 Battery
- C22: value 100n -> 10u; footprint Capacitor_SMD:C_0402_1005Metric -> Capacitor_SMD:C_0805_2012Metric
- C23, C24: value 47u -> 2.2n; footprint Capacitor_SMD:C_0805_2012Metric -> Capacitor_SMD:C_0402_1005Metric
- C25, C26: value 100n -> 1u; footprint Capacitor_SMD:C_0402_1005Metric -> Capacitor_SMD:C_0603_1608Metric
- C32: value 2.2u -> 100n; footprint Capacitor_SMD:C_1206_3216Metric -> Capacitor_SMD:C_0402_1005Metric; moved to B.Cu
- C33: moved to B.Cu
- D4: value LED_Dual_AAKK -> Zener 20V; footprint PiCard:LED-ARRAY-SMD_4P-L3.0-W1.5-L-FD -> Diode_SMD:D_SOD-323
- J3: footprint PiCard:TF-SMD_503398-1892 -> PiCard:SDCARD_MOLEX_503398-1892
- Q2: value DMP3013SFV -> DMN32D2LFB4; footprint Package_SON:Diodes_PowerDI3333-8 -> Package_DFN_QFN:Diodes_DFN1006-3; moved to B.Cu
- R14: value 1k -> 12k
- R16: value 15.8k -> 220k 1%
- R21: value 15.8k -> 953
- R23: value 49.9k -> 953
- R25: value 1k -> 12k; moved to F.Cu
- R26: value 5.1k -> 12k; moved to F.Cu
- R27: value 5.1k -> 120k
- R29: value 909k -> 4.7k 0.25W; footprint Resistor_SMD:R_0402_1005Metric -> Resistor_SMD:R_1206_3216Metric
- R30: value 12k -> 4.7k 0.25W; footprint Resistor_SMD:R_0402_1005Metric -> Resistor_SMD:R_1206_3216Metric
- R31, R32: value 200k -> 10k
- R33: value 499k -> 5.1k
- R34, R35: value 12k -> 3.3k
- R36: value 1k -> 5.1k
- SW1: value SW_DIP_x04 -> SW_Push; footprint PiCard:SW-SMD_8P-P1.27_EU-04KS -> PiCard:SW-SMD_L4.7-W3.5-P3.35-EH
- SYM1: value PiCard v2.2 -> PiCard v3.0
- U1: value MAX3232 -> ADM3101EACPZ; footprint Package_SO:TSSOP-16_4.4x5mm_P0.65mm -> PiCard:LFCSP-12-1EP_3x3mm_P0.5mm_EP1.3x1.3mm
- U10: value TPS2552 -> TVS2200DRV; footprint Package_TO_SOT_SMD:SOT-23-6 -> Package_SON:WSON-6-1EP_2x2mm_P0.65mm_EP1x1.6mm; moved to F.Cu
- U11: value TPD4EUSB30 -> TPS259470; footprint Package_SON:USON-10_2.5x1.0mm_P0.5mm -> PiCard:RPW0010A-MFG
- U12: value TPD4EUSB30 -> TPS259470; footprint Package_SON:USON-10_2.5x1.0mm_P0.5mm -> PiCard:RPW0010A-MFG; moved to B.Cu
- U13: value TPD4EUSB30 -> AP21510; footprint Package_SON:USON-10_2.5x1.0mm_P0.5mm -> Package_DFN_QFN:DFN-6-1EP_2x1.8mm_P0.5mm_EP1.2x1.6mm
- U15: value TS3USB221 -> AP21510; footprint Package_DFN_QFN:Texas_UQFN-10_1.5x2mm_P0.5mm -> Package_DFN_QFN:DFN-6-1EP_2x1.8mm_P0.5mm_EP1.2x1.6mm
- U16: value HD3SS3220 -> TPS259470; footprint PiCard:RNH0030A -> PiCard:RPW0010A-MFG
- U17: value TS3USB221 -> TPS259470; footprint Package_DFN_QFN:Texas_UQFN-10_1.5x2mm_P0.5mm -> PiCard:RPW0010A-MFG
- U18: value 74LVC1G07 -> TPD4EUSB30; footprint Package_TO_SOT_SMD:SOT-353_SC-70-5 -> Package_SON:USON-10_2.5x1.0mm_P0.5mm
- U2: value SN74AHC123A -> 74HC123PW
- U5: value TPS2553 -> AP2191W; footprint Package_TO_SOT_SMD:SOT-23-6 -> Package_TO_SOT_SMD:SOT-23-5
- U9: value DS1307Z+ -> TVS2200DRV; footprint Package_SO:SOIC-8_3.9x4.9mm_P1.27mm -> Package_SON:WSON-6-1EP_2x2mm_P0.65mm_EP1x1.6mm; moved to F.Cu
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- renumbered C15 to C10, C16 to C11, C17 to C12, C19 to C13, C20 to C14, C18 to C15, C21 to C16, C7 to C5, C8 to C6, C6 to C7, C9 to C8, C14 to C9, D3 to D2, R22 to R11, R24 to R12, R15 to R13, R5 to R3, R6 to R5, R7 to R6, R9 to R8, U14 to U19, U8 to U6, U6 to U7
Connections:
- BT1 pad 2: GND -> Net-(BT1--)
- C1 pad 1: GND -> Net-(U1-C1+)
- C1 pad 2: +3.3V -> Net-(U1-C1-)
- C2 pad 1: Net-(U1-C1+) -> +3.3V
- C2 pad 2: Net-(U1-C1-) -> Net-(U1-V+)
- C22 pad 1: GND -> +5V
- C22 pad 2: +5V -> GND
- C23 pad 1: GND -> Net-(U16-dVdt)
- C23 pad 2: +5V -> GND
- C24 pad 1: GND -> Net-(U17-dVdt)
- C24 pad 2: +5V -> GND
- C25 pad 2: +5V -> M2_3.3V
- C26 pad 2: +3.3V -> M2_3.3V
- C27 pad 1: /USB/LEFT_USB3_TX1P -> Net-(U22-VBIAS)
- C27 pad 2: /USB/TX1N -> GND
- C28 pad 1: /USB/LEFT_USB3_TX1N -> GND
- C28 pad 2: /USB/TX1P -> Net-(U23-VBIAS)
- C3 pad 1: Net-(U1-C2+) -> Net-(U1-V-)
- C3 pad 2: Net-(U1-C2-) -> GND
- C30 pad 1: /USB/LEFT_USB3_TX2P -> GND
- C30 pad 2: /USB/TX2N -> +3.3V
- C31 pad 1: /USB/LEFT_USB3_TX2N -> /USB/USB1_SS_TX1-
- C31 pad 2: /USB/TX2P -> /USB/MUX1_TX1-
- C32 pad 1: GND -> /USB/USB0_SS_TX1-
- C32 pad 2: PD_VBUS -> /USB/MUX0_TX1-
- C33 pad 1: GND -> /USB/USB1_SS_TX1+
- C33 pad 2: +5V -> /USB/MUX1_TX1+
- C34 pad 1: GND -> /USB/USB0_SS_TX1+
- C34 pad 2: +3.3V -> /USB/MUX0_TX1+
- C4 pad 1: Net-(U1-VS+) -> Net-(U1-C2+)
- C4 pad 2: GND -> Net-(U1-C2-)
- ComputeModule1 pad 101: unconnected-(ComputeModule1B-USB_OTG_ID-Pad101) -> CM_USB_OTG_ID
- ComputeModule1 pad 103: CM_USB2_N -> CM_USB2_D-
- ComputeModule1 pad 105: CM_USB2_P -> CM_USB2_D+
- ComputeModule1 pad 128: unconnected-(ComputeModule1B-CAM0_D0_N-Pad128) -> CM_USB3_0_SS_RX-
- ComputeModule1 pad 130: unconnected-(ComputeModule1B-CAM0_D0_P-Pad130) -> CM_USB3_0_SS_RX+
- ComputeModule1 pad 134: unconnected-(ComputeModule1B-CAM0_D1_N-Pad134) -> CM_USB3_0_HS_D+
- ComputeModule1 pad 136: unconnected-(ComputeModule1B-CAM0_D1_P-Pad136) -> CM_USB3_0_HS_D-
- ComputeModule1 pad 140: unconnected-(ComputeModule1B-CAM0_C_N-Pad140) -> CM_USB3_0_SS_TX-
- ComputeModule1 pad 142: unconnected-(ComputeModule1B-CAM0_C_P-Pad142) -> CM_USB3_0_SS_TX+
- ComputeModule1 pad 151: /Module B/HDMI0_CEC -> unconnected-(ComputeModule1B-HDMI0_CEC-Pad151)
- ComputeModule1 pad 153: /Module B/HDMI0_HOT_PLUG -> unconnected-(ComputeModule1B-HDMI0_HOTPLUG-Pad153)
- ComputeModule1 pad 157: CM_USB3_RX_N -> CM_USB3_1_SS_RX-
- ComputeModule1 pad 159: CM_USB3_RX_P -> CM_USB3_1_SS_RX+
- ComputeModule1 pad 163: CM_USB3_USB2_P -> CM_USB3_1_HS_D+
- ComputeModule1 pad 165: CM_USB3_USB2_N -> CM_USB3_1_HS_D-
- ComputeModule1 pad 169: CM_USB3_TX_N -> CM_USB3_1_SS_TX+
- ComputeModule1 pad 170: /Module B/HDMI0_TX2_P -> unconnected-(ComputeModule1B-HDMI0_TX2_P-Pad170)
- ComputeModule1 pad 171: CM_USB3_TX_P -> CM_USB3_1_SS_TX-
- ComputeModule1 pad 172: /Module B/HDMI0_TX2_N -> unconnected-(ComputeModule1B-HDMI0_TX2_N-Pad172)
- ComputeModule1 pad 176: /Module B/HDMI0_TX1_P -> unconnected-(ComputeModule1B-HDMI0_TX1_P-Pad176)
- ComputeModule1 pad 178: /Module B/HDMI0_TX1_N -> unconnected-(ComputeModule1B-HDMI0_TX1_N-Pad178)
- ComputeModule1 pad 182: /Module B/HDMI0_TX0_P -> unconnected-(ComputeModule1B-HDMI0_TX0_P-Pad182)
- ComputeModule1 pad 184: /Module B/HDMI0_TX0_N -> unconnected-(ComputeModule1B-HDMI0_TX0_N-Pad184)
- ComputeModule1 pad 188: /Module B/HDMI0_CLK_P -> unconnected-(ComputeModule1B-HDMI0_CLK_P-Pad188)
- ComputeModule1 pad 190: /Module B/HDMI0_CLK_N -> unconnected-(ComputeModule1B-HDMI0_CLK_N-Pad190)
- ComputeModule1 pad 199: /Module B/HDMI0_SDA -> unconnected-(ComputeModule1B-HDMI0_SDA-Pad199)
- ComputeModule1 pad 200: /Module B/HDMI0_SCL -> unconnected-(ComputeModule1B-HDMI0_SCL-Pad200)
- ComputeModule1 pad 21: /Module A/GREEN_LED_K -> CM_ACT_LED
- ComputeModule1 pad 25: unconnected-(ComputeModule1A-GPIO21-Pad25) -> CM_SPI1_SCLK
- ComputeModule1 pad 26: unconnected-(ComputeModule1A-GPIO19-Pad26) -> CM_SPI1_SIO1
- ComputeModule1 pad 27: unconnected-(ComputeModule1A-GPIO20-Pad27) -> CM_SPI1_SIO0
- ComputeModule1 pad 28: unconnected-(ComputeModule1A-GPIO13-Pad28) -> CM_UART4_RX
- ComputeModule1 pad 30: unconnected-(ComputeModule1A-GPIO6-Pad30) -> MCU_SWDCLK
- ComputeModule1 pad 34: unconnected-(ComputeModule1A-GPIO5-Pad34) -> CM_I2C2_SCL
- ComputeModule1 pad 35: unconnected-(ComputeModule1A-ID_SC-Pad35) -> CM_ID_SC
- ComputeModule1 pad 36: unconnected-(ComputeModule1A-ID_SD-Pad36) -> CM_ID_SD
- ComputeModule1 pad 37: unconnected-(ComputeModule1A-GPIO7-Pad37) -> MCU_SWDIO
- ComputeModule1 pad 38: unconnected-(ComputeModule1A-GPIO11-Pad38) -> MCU_nRST
- ComputeModule1 pad 39: unconnected-(ComputeModule1A-GPIO8-Pad39) -> CM_UART3_TX
- ComputeModule1 pad 40: unconnected-(ComputeModule1A-GPIO9-Pad40) -> CM_UART3_RX
- ComputeModule1 pad 48: unconnected-(ComputeModule1A-GPIO27-Pad48) -> CM_PWR_EN
- ComputeModule1 pad 49: unconnected-(ComputeModule1A-GPIO18-Pad49) -> CM_SPI1_CSN0
- ComputeModule1 pad 54: unconnected-(ComputeModule1A-GPIO4-Pad54) -> CM_I2C2_SDA
- ComputeModule1 pad 56: RTC_SCL -> CM_I2C1_SCL
- ComputeModule1 pad 58: RTC_SDA -> CM_I2C1_SDA
- ComputeModule1 pad 92: unconnected-(ComputeModule1A-RUN_PG-Pad92) -> CM_PWR_BUTTON
- ComputeModule1 pad 95: Net-(ComputeModule1A-nPI_LED_PWR) -> CM_PWR_LED
- D4 pad 1: +3.3V -> Net-(D4-K)
- D4 pad 2: +3.3V -> +5V
- J4 pad 10: unconnected-(J4-DAS/~{DSS}/~{LED1}-Pad10) -> M2_LED
- J4 pad 68: unconnected-(J4-SUSCLK-Pad68) -> M2_SUSCLK
- J5 pad A10: /USB/RX1N -> /USB/USB1_SS_RX2-
- J5 pad A11: /USB/RX1P -> /USB/USB1_SS_RX2+
- J5 pad A2: /USB/LEFT_USB3_TX2P -> /USB/USB1_SS_TX1+
- J5 pad A3: /USB/LEFT_USB3_TX2N -> /USB/USB1_SS_TX1-
- J5 pad A4: /USB/USB3_VBUS -> USB1_VBUS
- J5 pad A5: /USB/CC2 -> /USB/USB1_CC1
- J5 pad A6: /USB/LEFT_USB2_P -> /USB/USB1_DP
- J5 pad A7: /USB/LEFT_USB2_N -> /USB/USB1_DN
- J5 pad A9: /USB/USB3_VBUS -> USB1_VBUS
- J5 pad B10: /USB/RX2N -> /USB/USB1_SS_RX1-
- J5 pad B11: /USB/RX2P -> /USB/USB1_SS_RX1+
- J5 pad B2: /USB/LEFT_USB3_TX1P -> /USB/USB1_SS_TX2+
- J5 pad B3: /USB/LEFT_USB3_TX1N -> /USB/USB1_SS_TX2-
- J5 pad B4: /USB/USB3_VBUS -> USB1_VBUS
- J5 pad B5: /USB/CC1 -> /USB/USB1_CC2
- J5 pad B6: /USB/LEFT_USB2_P -> /USB/USB1_DP
- J5 pad B7: /USB/LEFT_USB2_N -> /USB/USB1_DN
- J5 pad B9: /USB/USB3_VBUS -> USB1_VBUS
- J6 pad A10: unconnected-(J6-RX2--PadA10) -> /USB/USB0_SS_RX2-
- J6 pad A11: unconnected-(J6-RX2+-PadA11) -> /USB/USB0_SS_RX2+
- J6 pad A2: unconnected-(J6-TX1+-PadA2) -> /USB/USB0_SS_TX1+
- J6 pad A3: unconnected-(J6-TX1--PadA3) -> /USB/USB0_SS_TX1-
- J6 pad A4: PD_VBUS -> USB0_VBUS
- J6 pad A5: PD_CC1 -> /USB/USB0_CC1
- J6 pad A6: /USB/RIGHT_USB2_P -> /USB/USB0_DP
- J6 pad A7: /USB/RIGHT_USB2_N -> /USB/USB0_DN
- J6 pad A9: PD_VBUS -> USB0_VBUS
- J6 pad B10: unconnected-(J6-RX1--PadB10) -> /USB/USB0_SS_RX1-
- J6 pad B11: unconnected-(J6-RX1+-PadB11) -> /USB/USB0_SS_RX1+
- J6 pad B2: unconnected-(J6-TX2+-PadB2) -> /USB/USB0_SS_TX2+
- J6 pad B3: unconnected-(J6-TX2--PadB3) -> /USB/USB0_SS_TX2-
- J6 pad B4: PD_VBUS -> USB0_VBUS
- J6 pad B5: PD_CC2 -> /USB/USB0_CC2
- J6 pad B6: /USB/RIGHT_USB2_P -> /USB/USB0_DP
- J6 pad B7: /USB/RIGHT_USB2_N -> /USB/USB0_DN
- J6 pad B9: PD_VBUS -> USB0_VBUS
- Q2 pad 1: PD_VBUS -> USB0_DISCHARGE
- Q2 pad 2: PD_VBUS -> GND
- Q2 pad 3: PD_VBUS -> Net-(Q2-D)
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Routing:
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- added copper zone on B.Cu, net +5V
- added copper zone on In3.Cu, net GND
- added copper zone on In4.Cu, net GND
- added copper zone on B.Cu, net USB0_VBUS
- added copper zone on F.Cu, net USB0_VBUS
- added copper zone on B.Cu, net USB1_VBUS
- added copper zone on F.Cu, net USB1_VBUS
- removed copper zone on B.Cu, net /USB/USB3_VBUS
- removed copper zone on In1.Cu, net /USB/USB3_VBUS
- removed copper zone on In2.Cu, net /USB/USB3_VBUS
- removed copper zone on F.Cu, net PD_VBUS
- removed copper zone on F.Cu, net VBUS
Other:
- copper layers 4 -> 6
- board text added: "1 USB0 2 USB1 3 RPIBOOT 4 Serial LED"
- board text added: "Console"
- board text removed: "JLCJLCJLCJLC"
- board text removed: "OFF OFF OFF OFF"
- board text removed: "ON ON ON ON"
- board text removed: "RS232"
- board text removed: "USB3 USB2 RPIBOOT RS232 LED"
